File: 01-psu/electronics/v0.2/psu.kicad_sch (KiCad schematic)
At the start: 25 parts, among them IC1 ISOLATED_DC-DC_CONV, J1 Barrel_Jack_Switch, J13 Conn_01x03, J2 Conn_02x08_Odd_Even, J3 Conn_02x08_Odd_Even, J4 Conn_02x08_Odd_Even, J5 Conn_02x08_Odd_Even

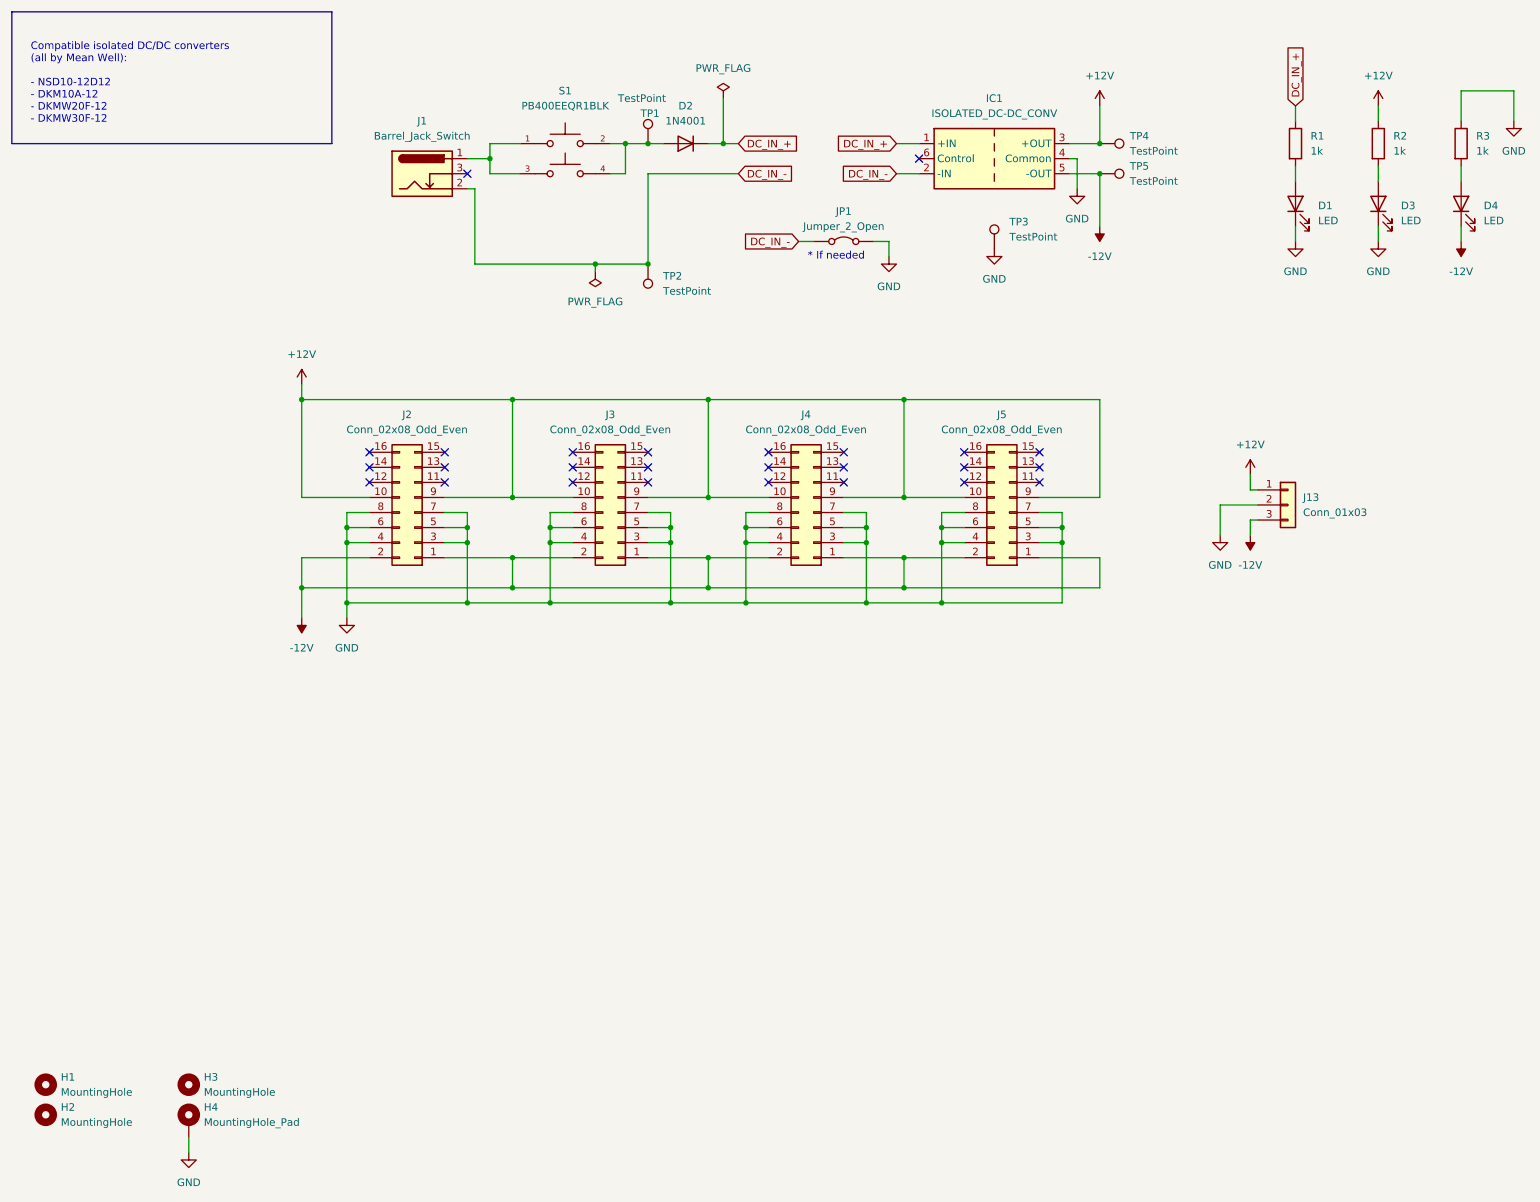
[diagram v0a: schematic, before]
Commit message: PSU v0.2 and fixed crosstalk on VCA
- added PSU v0.2
- VCA had a crosstalk issue. The input signal got superimposed on the output. The current solution is to move the input voltage divider on the core board as close to the input pin header connection as possible. Additionally, I added the 100k resistor as a THT component to the UI board. Only one of the 100k resistors is needed, but I added both for testing purposes.
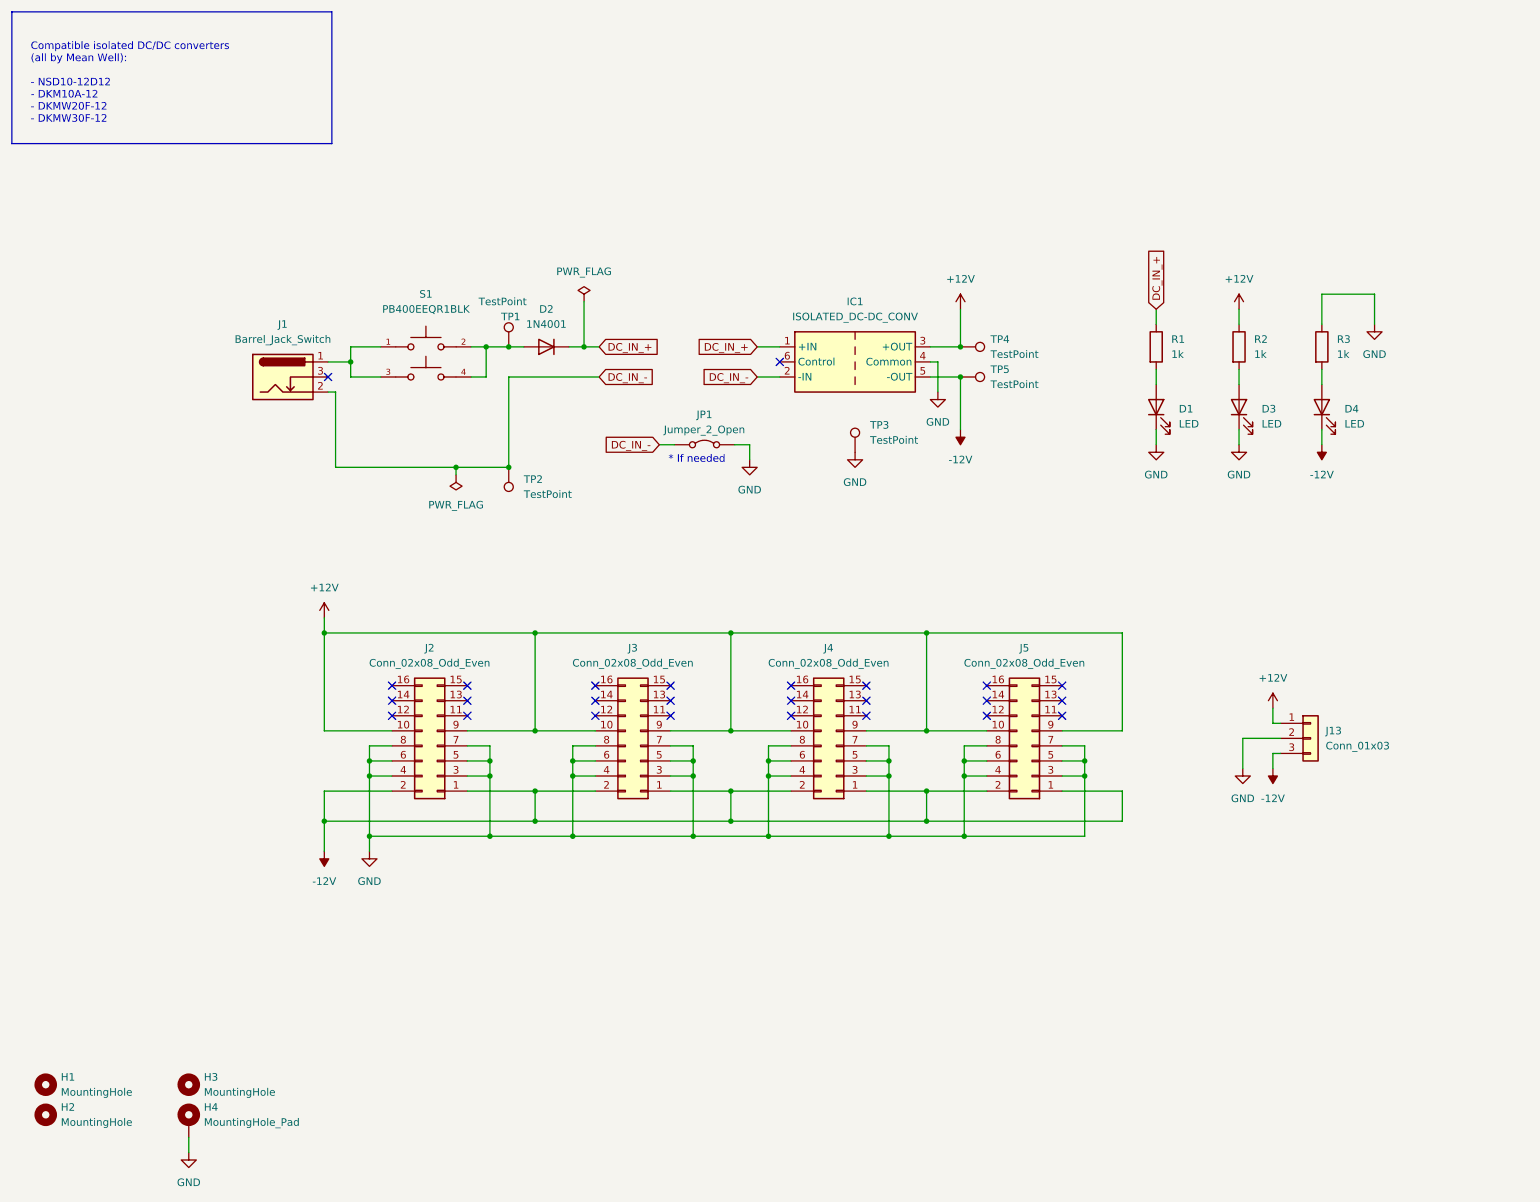
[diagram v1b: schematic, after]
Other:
- moved on the sheet: D1, D2, D3, D4, IC1, J1, J13, J2, J3, J4, J5, JP1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

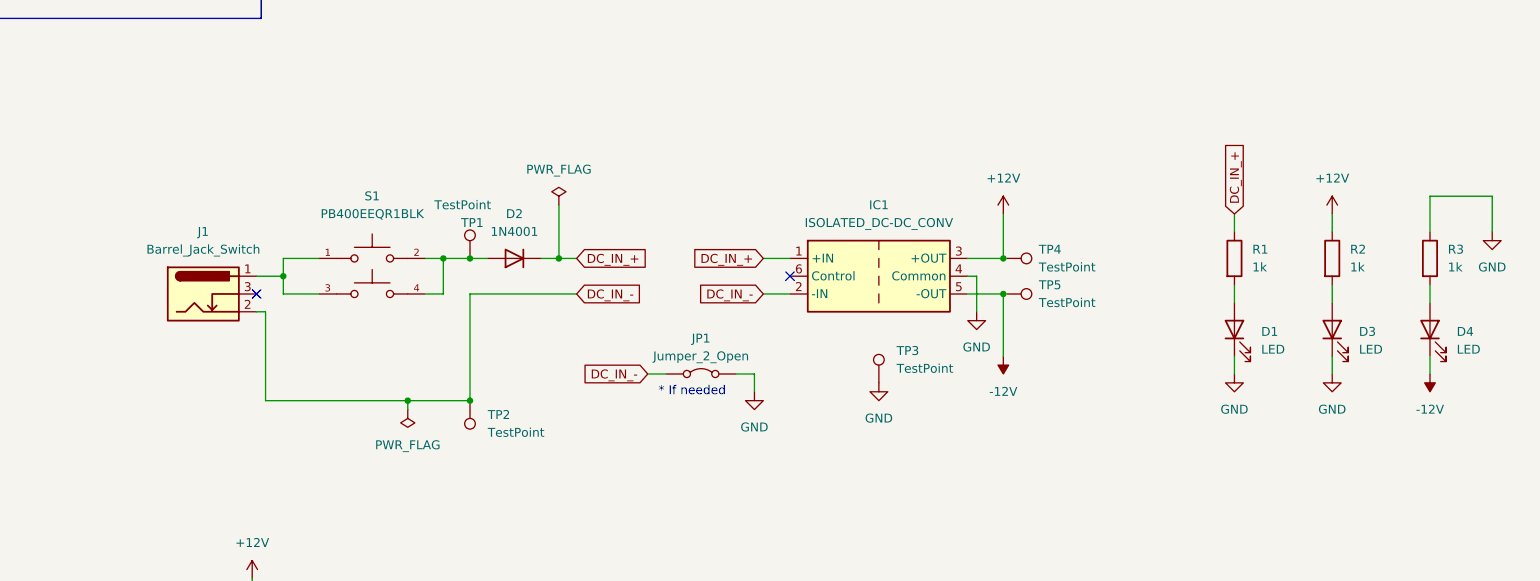
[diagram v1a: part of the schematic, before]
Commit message: Swapped DC/DC converter from back to front on PSU PCB
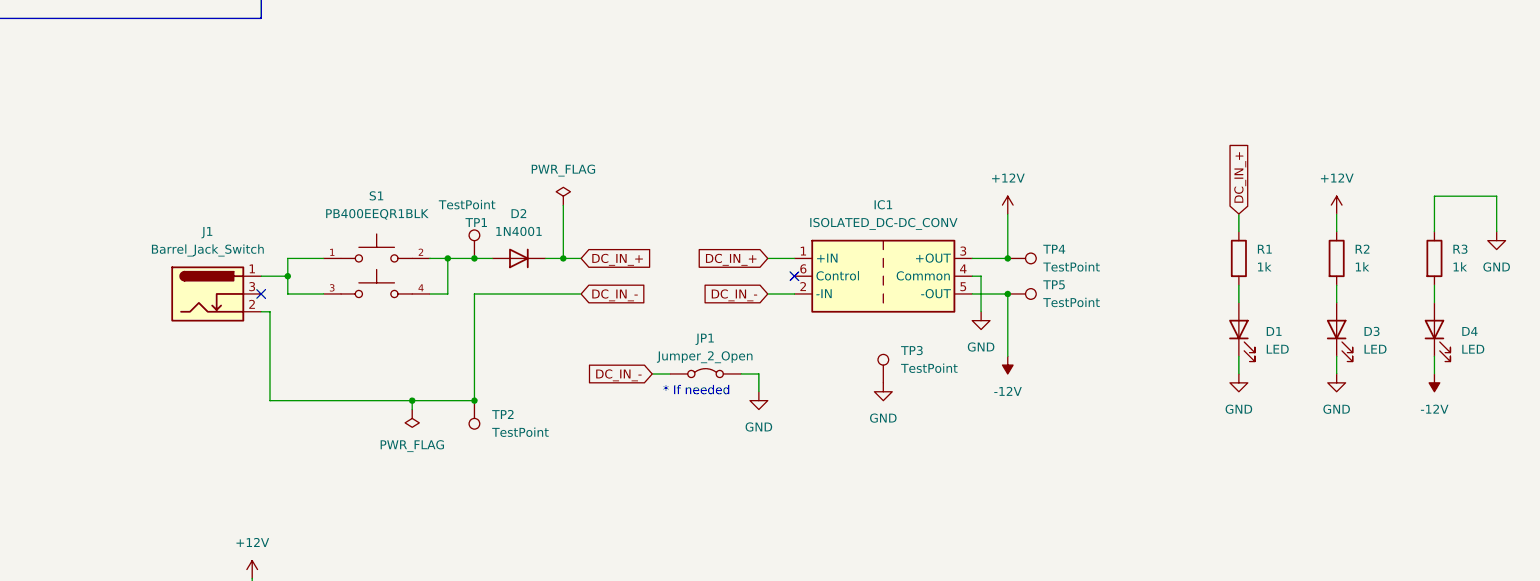
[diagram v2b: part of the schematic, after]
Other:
- moved on the sheet: D1, D2, D3, D4, IC1, J1, JP1, R1, R2, R3, S1, TP1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
